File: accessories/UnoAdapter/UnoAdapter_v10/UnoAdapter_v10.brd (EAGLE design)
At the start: 68.6 x 53.3 mm, 10 parts, among them X1 DC21MMX

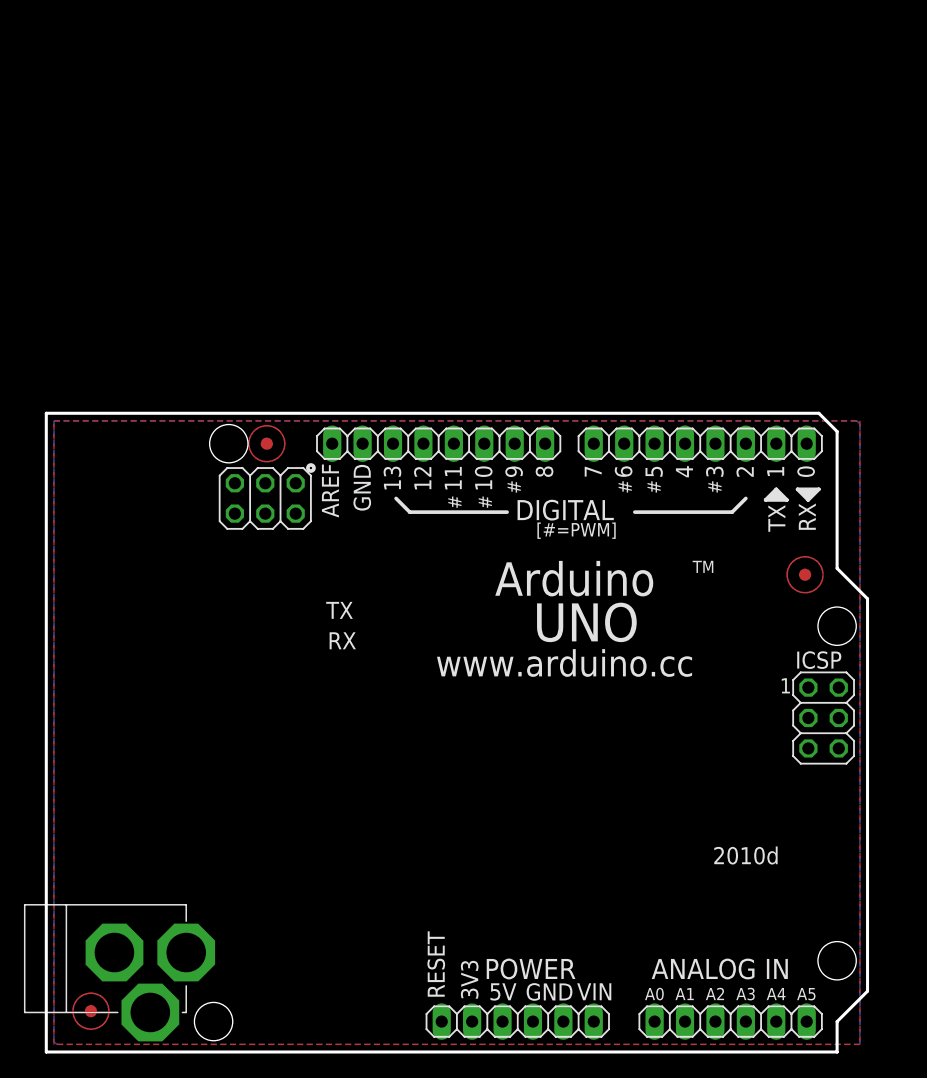
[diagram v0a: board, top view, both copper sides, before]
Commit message: More work on Uno Adapter
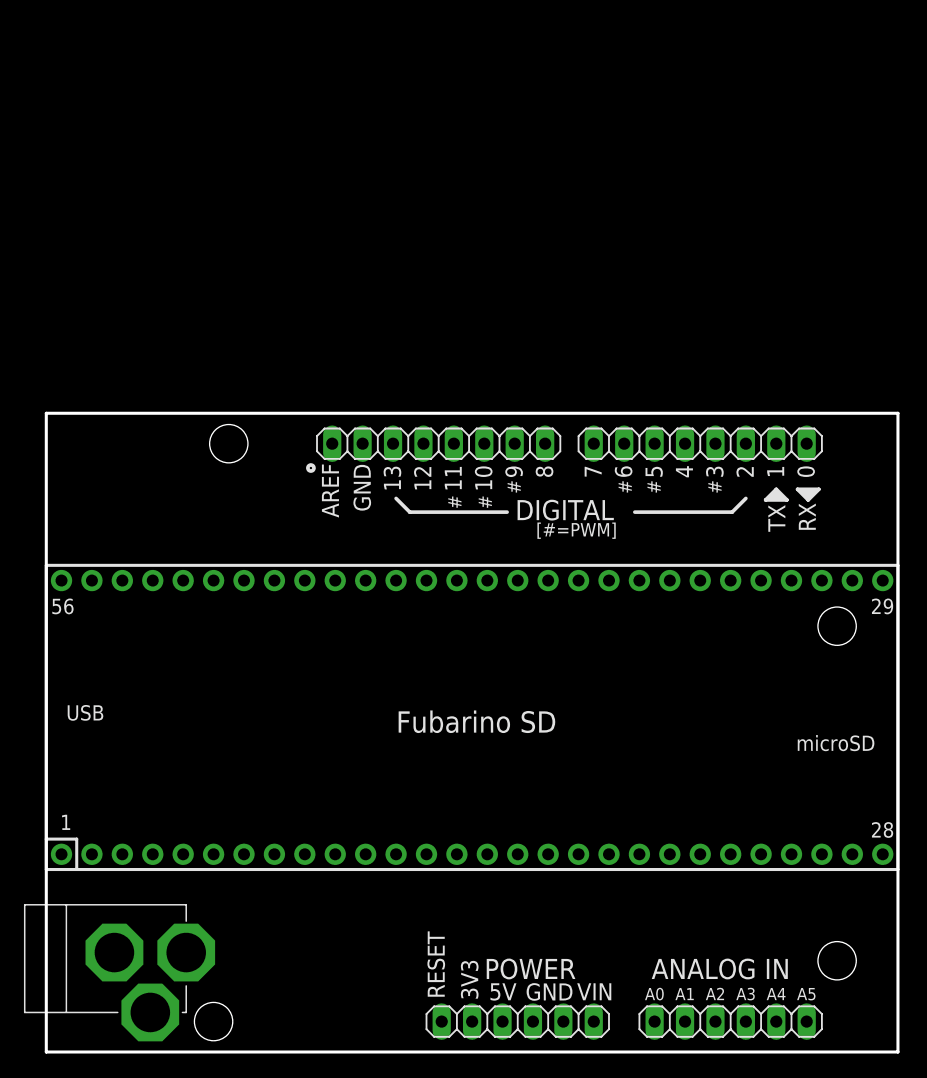
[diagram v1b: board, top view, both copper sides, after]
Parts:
- removed ICSP, ICSP1: ICSP, pinhead:2X03
- removed U$3, U$4, U$6: FIDUCIALMOUNT, SmartPrj:FIDUCIA-MOUNT
- added U$1: FUBARINO_SD, SchmalzHausPublic:FUBARINO_SD
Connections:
- removed net MISO2: ICSP1.1
- removed net N$12: POWER.1
- removed net PWRIN: X1.2
- removed net RESET2: ICSP1.5
- removed net SCK2: ICSP1.3
- new net N$1: U$1.1
- new net N$10: U$1.10
- new net N$11: U$1.11
- new net N$13: U$1.12
- new net N$14: U$1.13
- new net N$15: U$1.14
- new net N$16: U$1.15
- new net N$17: U$1.16
- new net N$18: U$1.17
- new net N$19: U$1.18
- new net N$20: U$1.19
- new net N$21: U$1.20
- new net N$22: U$1.21
- new net N$23: U$1.22
- new net N$24: U$1.23
- new net N$25: U$1.24
- new net N$26: U$1.25
- new net N$27: U$1.26
- new net N$28: U$1.27
- new net N$33: U$1.53
- new net N$34: U$1.52
- new net N$35: U$1.51
- new net N$36: U$1.50
- new net N$37: U$1.49
- new net N$38: U$1.48
- new net N$39: U$1.47
- new net N$4: U$1.4
- new net N$40: U$1.46
- new net N$41: U$1.45
- new net N$42: U$1.44
- new net N$43: U$1.43
- new net N$44: U$1.42
- new net N$48: U$1.38
- new net N$49: U$1.37
- new net N$5: U$1.5
- new net N$50: U$1.36
- new net N$51: U$1.35
- new net N$52: U$1.34
- new net N$53: U$1.33
- new net N$54: U$1.32
- new net N$55: U$1.31
- new net N$56: U$1.30
- new net N$6: U$1.6
- new net N$7: U$1.7
- new net N$8: U$1.8
- new net N$9: U$1.9
- net +3V3: now also U$1.3, U$1.40, U$1.54
- net +5V: no longer ICSP.2, ICSP1.2
- net GND: now also U$1.2, U$1.28, U$1.29, U$1.41, U$1.55; no longer ICSP.6, ICSP1.6
- net MISO: no longer ICSP.1
- net MOSI: no longer ICSP.4
- net RESET: now also POWER.1, U$1.39; no longer ICSP.5
- net SCK: no longer ICSP.3
- net VIN: now also U$1.56, X1.2
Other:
- board size 68.6 x 53.3 mm -> 71.1 x 53.3 mm
- board text removed: "2010d"
- board text removed: "ARDUINO is a registered trademark by Arduino LLC, Boston, MA, USA"
- board text removed: "ATMEGA328"
- board text removed: "Arduino"
- board text removed: "Arduino may make changes to specifications and product descriptions at any time, without notice. The Customer must not"
- board text removed: "ITALY"
- board text removed: "L"
- board text removed: "MADE IN"
- board text removed: "PC1"
- board text removed: "PC2"
- board text removed: "REGARDING PRODUCTS, INCLUDING BUT NOT LIMITED TO, ANY IMPLIED WARRANTIES OF MERCHANTABILITY OR FITNESS FOR A PARTICULAR PURPOSE"
- board text removed: "Reference Designs ARE PROVIDED "AS IS" AND "WITH ALL FAULTS". Arduino DISCLAIMS ALL OTHER WARRANTIES, EXPRESS OR IMPLIED,"
- board text removed: "TM"
- board text removed: "The product information on the Web Site or Materials is subject to change without notice. Do not finalize a design with this information."
- board text removed: "UNO"
- board text removed: "rely on the absence or characteristics of any features or instructions marked "reserved" or "undefined." Arduino reserves"
- board text removed: "these for future definition and shall have no responsibility whatsoever for conflicts or incompatibilities arising from future changes to them."
- board text removed: "www.arduino.cc"

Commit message: Added Fubarino Mini to board.
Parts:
- added U$2: FUBARINO_MINI, SchmalzHausPublic:FUBARINO_MINI
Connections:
- removed net N$1: U$1.1
- new net N$30: U$2.36
- new net N$31: U$2.35
- new net N$32: U$2.34
- new net N$45: U$2.33
- new net N$46: U$2.32
- new net N$47: U$2.31
- new net N$57: U$2.30
- new net N$58: U$2.29
- new net N$59: U$2.28
- new net N$60: U$2.27
- new net N$61: U$2.26
- new net N$62: U$2.25
- new net N$63: U$2.24
- new net N$64: U$2.23
- new net N$65: U$2.22
- new net N$66: U$2.21
- new net N$70: U$2.4
- new net N$71: U$2.5
- new net N$72: U$2.6
- new net N$73: U$2.7
- new net N$74: U$2.8
- new net N$75: U$2.9
- new net N$76: U$2.10
- new net N$77: U$2.11
- new net N$78: U$2.12
- new net N$79: U$2.13
- new net N$80: U$2.14
- new net N$81: U$2.15
- new net N$82: U$2.16
- new net N$83: U$2.17
- new net N$84: U$2.18
- new net N$85: U$2.19
- new net N$86: U$2.20
- net +3V3: now also U$2.3, U$2.38
- net +5V: now also U$1.1, U$2.1
- net GND: now also U$2.2, U$2.37, U$2.39
- net VIN: now also U$2.40
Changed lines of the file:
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@@
 </element>
 <element name="U$1" library="SchmalzHausPublic" package="FUBARINO_SD" value="FUBARINO_SD" x="35.56" y="27.94"/>
+<element name="U$2" library="SchmalzHausPublic" package="FUBARINO_MINI" value="FUBARINO_MINI" x="25.4" y="27.94"/>
 </elements>
 <signals>
 <signal name="+5V">
 <contactref element="POWER" pad="3"/>
+<contactref element="U$2" pad="1"/>
+<contactref element="U$1" pad="1"/>
+<wire x1="1.27" y1="16.51" x2="38.1" y2="2.54" width="0" layer="19" extent="1-1"/>
+<wire x1="1.27" y1="20.32" x2="1.27" y2="16.51" width="0" layer="19" extent="1-1"/>
 </signal>
 <signal name="GND">
@@
 <contactref element="U$1" pad="55"/>
 <contactref element="U$1" pad="2"/>
+<contactref element="U$2" pad="2"/>
+<contactref element="U$2" pad="37"/>
+<contactref element="U$2" pad="39"/>
+<wire x1="69.85" y1="16.51" x2="69.85" y2="39.37" width="0" layer="19" extent="1-1"/>
+<wire x1="43.18" y1="2.54" x2="69.85" y2="16.51" width="0" layer="19" extent="1-1"/>
+<wire x1="40.64" y1="2.54" x2="43.18" y2="2.54" width="0" layer="19" extent="1-1"/>
+<wire x1="39.37" y1="39.37" x2="69.85" y2="39.37" width="0" layer="19" extent="1-1"/>
+<wire x1="26.416" y1="50.8" x2="39.37" y2="39.37" width="0" layer="19" extent="1-1"/>
+<wire x1="3.81" y1="39.37" x2="26.416" y2="50.8" width="0" layer="19" extent="1-1"/>
+<wire x1="3.81" y1="16.51" x2="3.81" y2="39.37" width="0" layer="19" extent="1-1"/>
+<wire x1="5.6896" y1="8.3058" x2="3.81" y2="16.51" width="0" layer="19" extent="1-1"/>
+<wire x1="8.6868" y1="3.302" x2="5.6896" y2="8.3058" width="0" layer="19" extent="1-1"/>
+<wire x1="8.89" y1="35.56" x2="8.6868" y2="3.302" width="0" layer="19" extent="1-1"/>
+<wire x1="3.81" y1="35.56" x2="8.89" y2="35.56" width="0" layer="19" extent="1-1"/>
+<wire x1="3.81" y1="20.32" x2="3.81" y2="35.56" width="0" layer="19" extent="1-1"/>
 </signal>
 <signal name="AREF">
@@
 <contactref element="X1" pad="2"/>
 <contactref element="U$1" pad="56"/>
+<contactref element="U$2" pad="40"/>
 <wire x1="11.684" y1="8.3058" x2="45.72" y2="2.54" width="0" layer="19" extent="1-1"/>
+<wire x1="1.27" y1="35.56" x2="11.684" y2="8.3058" width="0" layer="19" extent="1-1"/>
 <wire x1="1.27" y1="39.37" x2="11.684" y2="8.3058" width="0" layer="19" extent="1-1"/>
 </signal>
@@
 <contactref element="U$1" pad="3"/>
 <contactref element="U$1" pad="40"/>
+<contactref element="U$2" pad="3"/>
+<contactref element="U$2" pad="38"/>
 <wire x1="6.35" y1="39.37" x2="41.91" y2="39.37" width="0" layer="19" extent="1-1"/>
 <wire x1="6.35" y1="16.51" x2="6.35" y2="39.37" width="0" layer="19" extent="1-1"/>
+<wire x1="6.35" y1="35.56" x2="6.35" y2="16.51" width="0" layer="19" extent="1-1"/>
+<wire x1="6.35" y1="20.32" x2="6.35" y2="35.56" width="0" layer="19" extent="1-1"/>
 <wire x1="35.56" y1="2.54" x2="6.35" y2="16.51" width="0" layer="19" extent="1-1"/>
 </signal>
@@
 <signal name="IO9">
 <contactref element="IOH" pad="2"/>
-</signal>
-<signal name="N$1">
-<contactref element="U$1" pad="1"/>
 </signal>
 <signal name="N$4">
@@
 <contactref element="U$1" pad="30"/>
 </signal>
+<signal name="N$30">
+<contactref element="U$2" pad="36"/>
+</signal>
+<signal name="N$31">
+<contactref element="U$2" pad="35"/>
+</signal>
+<signal name="N$32">
+<contactref element="U$2" pad="34"/>
+</signal>
+<signal name="N$45">
+<contactref element="U$2" pad="33"/>
+</signal>
+<signal name="N$46">
+<contactref element="U$2" pad="32"/>
+</signal>
+<signal name="N$47">
+<contactref element="U$2" pad="31"/>
+</signal>
+<signal name="N$57">
+<contactref element="U$2" pad="30"/>
+</signal>
+<signal name="N$58">
+<contactref element="U$2" pad="29"/>
+</signal>
+<signal name="N$59">
+<contactref element="U$2" pad="28"/>
+</signal>
+<signal name="N$60">
+<contactref element="U$2" pad="27"/>
+</signal>
+<signal name="N$61">
+<contactref element="U$2" pad="26"/>
+</signal>
+<signal name="N$62">
+<contactref element="U$2" pad="25"/>
+</signal>
+<signal name="N$63">
+<contactref element="U$2" pad="24"/>
+</signal>
+<signal name="N$64">
+<contactref element="U$2" pad="23"/>
+</signal>
+<signal name="N$65">
+<contactref element="U$2" pad="22"/>
+</signal>
+<signal name="N$66">
+<contactref element="U$2" pad="21"/>
+</signal>
+<signal name="N$70">
+<contactref element="U$2" pad="4"/>
+</signal>
+<signal name="N$71">
+<contactref element="U$2" pad="5"/>
+</signal>
+<signal name="N$72">
+<contactref element="U$2" pad="6"/>
+</signal>
+<signal name="N$73">
+<contactref element="U$2" pad="7"/>
+</signal>
+<signal name="N$74">
+<contactref element="U$2" pad="8"/>
+</signal>
+<signal name="N$75">
+<contactref element="U$2" pad="9"/>
+</signal>
+<signal name="N$76">
+<contactref element="U$2" pad="10"/>
+</signal>
+<signal name="N$77">
+<contactref element="U$2" pad="11"/>
+</signal>
+<signal name="N$78">
+<contactref element="U$2" pad="12"/>
+</signal>
+<signal name="N$79">
+<contactref element="U$2" pad="13"/>
+</signal>
+<signal name="N$80">
+<contactref element="U$2" pad="14"/>
+</signal>
+<signal name="N$81">
+<contactref element="U$2" pad="15"/>
+</signal>
+<signal name="N$82">
+<contactref element="U$2" pad="16"/>
+</signal>
+<signal name="N$83">
+<contactref element="U$2" pad="17"/>
+</signal>
+<signal name="N$84">
+<contactref element="U$2" pad="18"/>
+</signal>
+<signal name="N$85">
+<contactref element="U$2" pad="19"/>
+</signal>
+<signal name="N$86">
+<contactref element="U$2" pad="20"/>
+</signal>
 </signals>

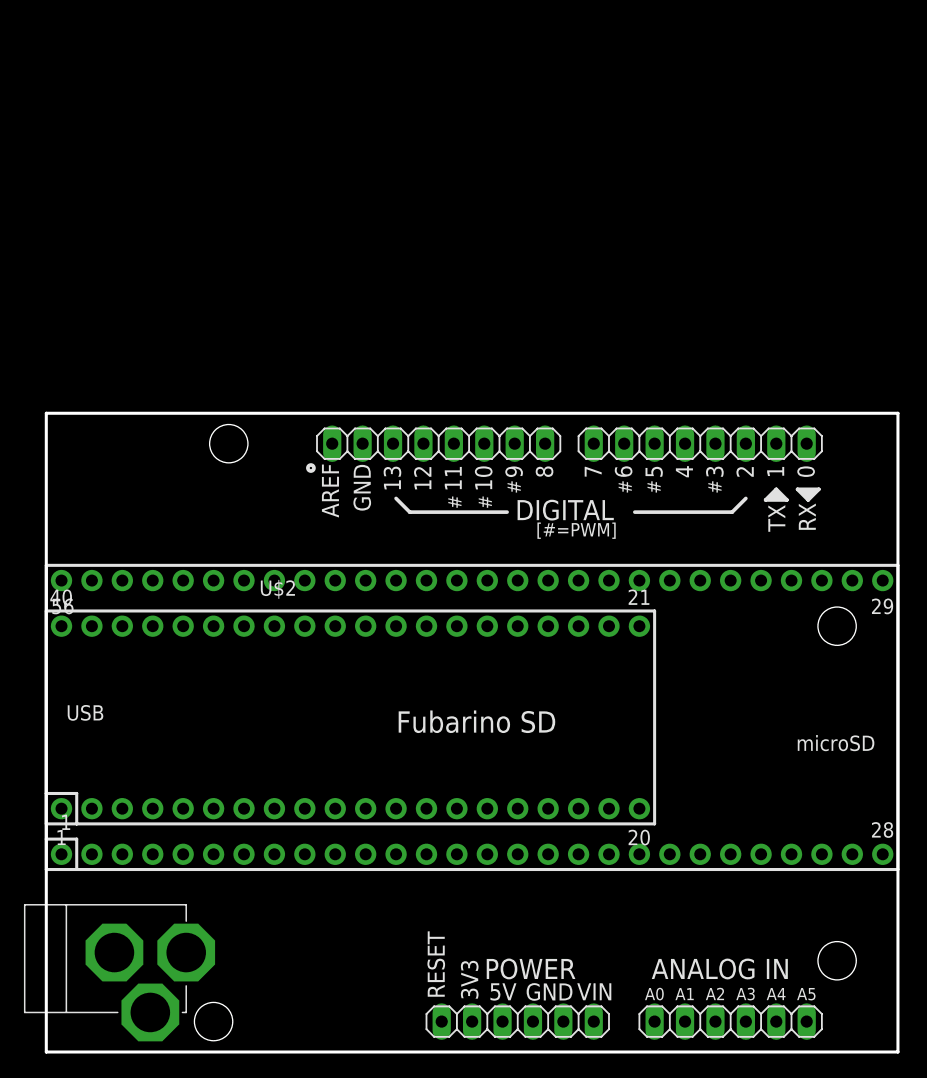
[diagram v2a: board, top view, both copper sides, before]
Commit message: Moved Fubarinos around, added regulator.
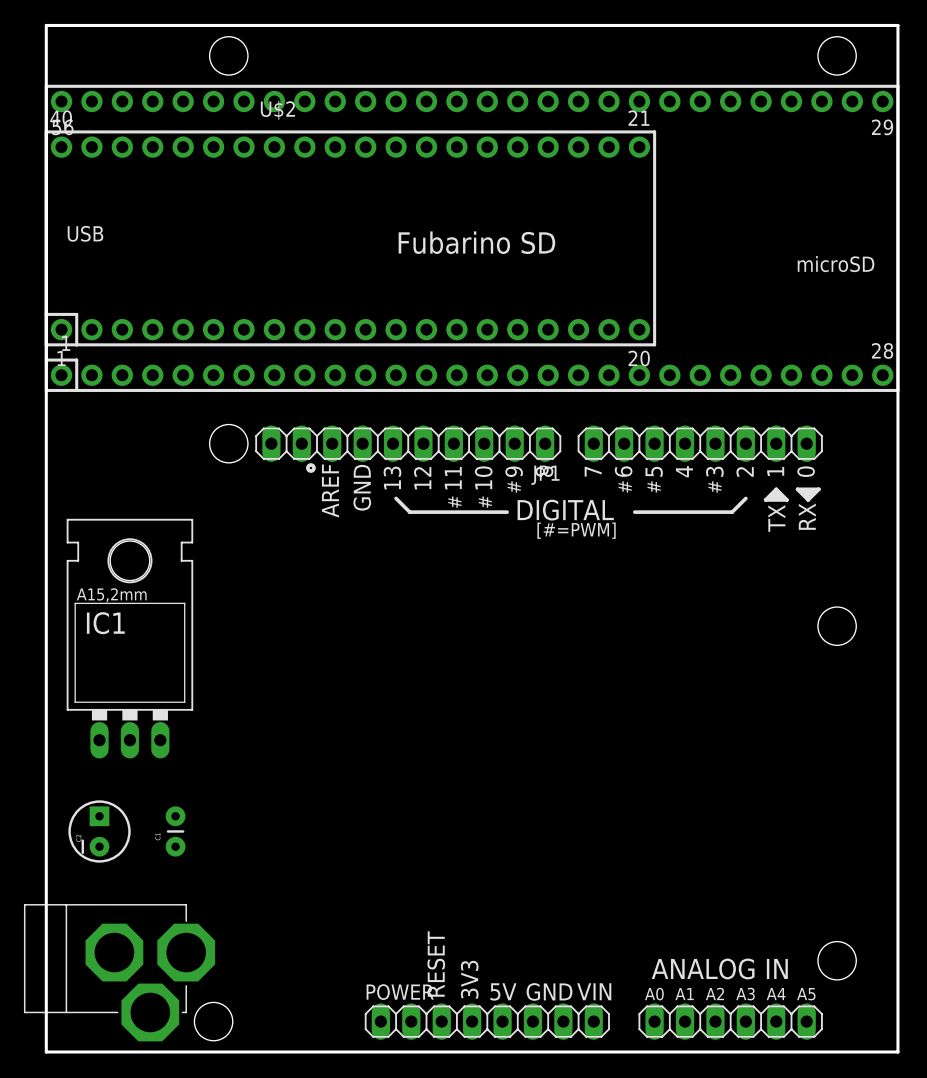
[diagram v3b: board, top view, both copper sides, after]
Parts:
- removed IOH: (no value), pinhead:1X08
- added C1: .1uF, SparkFun-Capacitors:CAP-PTH-SMALL
- added C2: 10uF, SparkFun-Capacitors:CPOL-RADIAL-10UF-25V
- added IC1: 7805, SparkFun-PowerIC:78XXL
- added JP1: (no value), pinhead:1X10
- POWER: device pinhead:1X06 -> pinhead:1X08
- moved U$1 40.0 mm to (35.6, 67.9)
- moved U$2 40.0 mm to (25.4, 67.9)
- moved POWER 2.54 mm to (36.8, 2.54)
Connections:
- new net AD4/SDA: JP1.9
- new net AD5/SCL: JP1.10
- net +3V3: now also POWER.4; no longer POWER.2
- net +5V: now also C1.1, IC1.OUT, POWER.2, POWER.5; no longer POWER.3
- net AREF: now also JP1.8; no longer IOH.8
- net GND: now also C1.2, C2.2, IC1.GND, JP1.7, POWER.6, POWER.7; no longer IOH.7, POWER.4, POWER.5
- net IO8: now also JP1.1; no longer IOH.1
- net IO9: now also JP1.2; no longer IOH.2
- net MISO: now also JP1.5; no longer IOH.5
- net MOSI: now also JP1.4; no longer IOH.4
- net RESET: now also POWER.3; no longer POWER.1
- net SCK: now also JP1.6; no longer IOH.6
- net SS: now also JP1.3; no longer IOH.3
- net VIN: now also C2.1, IC1.IN, POWER.8; no longer POWER.6
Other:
- board size 71.1 x 53.3 mm -> 71.1 x 85.7 mm
